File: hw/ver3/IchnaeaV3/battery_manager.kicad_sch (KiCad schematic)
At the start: 1 part, among them J4 BalanceConnector

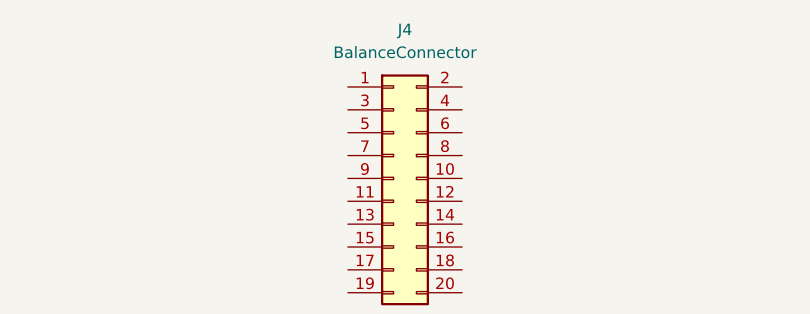
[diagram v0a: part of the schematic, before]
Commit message: Experiment with a new power stage layout
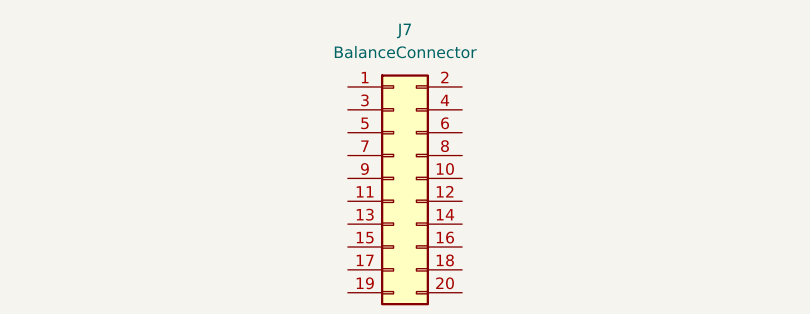
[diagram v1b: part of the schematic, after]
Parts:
- renumbered J4 to J7
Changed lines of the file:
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@@
 		(dnp no)
 		(fields_autoplaced yes)
-		(property "Reference" "J4"
+		(property "Reference" "J7"
 			(at 200.66 25.4 0)
 			(effects
@@
 			(project "IchnaeaV3"
 				(path "/93408532-1ffa-463d-873c-16289d2b7987/f8cdf9d7-add1-4ff8-8430-918a71e3d1f9/15949d39-4147-469d-a992-c4b48798ba19"
-					(reference "J4")
+					(reference "J7")
 					(unit 1)
 				)
